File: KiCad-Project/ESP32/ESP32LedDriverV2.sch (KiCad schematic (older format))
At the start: 25 parts, among them J1 Power, J2 LED Terminal, Q1 Q_PMOS_GDS, Q2 S8050, U1 INA219AxD, U2 R-78C5.0-1.0

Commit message: swap out 603 resistors for 805
Give us more room to work with if we have to fix something.
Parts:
- R1: footprint Resistor_SMD:R_0603_1608Metric -> Resistor_SMD:R_0805_2012Metric; JLCPCB_PNUM C25804 -> C17414; MFG_PNUM 0603WAF1002T5E -> 0805W8F1002T5E; PACKAGE 0603 -> 0805
- R2, R4, R5, R6, R7: footprint Resistor_SMD:R_0201_0603Metric -> Resistor_SMD:R_0805_2012Metric; JLCPCB_PNUM C25804 -> C17414; MFG_PNUM 0603WAF1002T5E -> 0805W8F1002T5E; PACKAGE 0603 -> 0805
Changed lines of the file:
@@
 F 0 "R1" H 1643 1046 50  0000 L CNN
 F 1 "10K" H 1643 955 50  0000 L CNN
-F 2 "Resistor_SMD:R_0603_1608Metric" V 1615 990 50  0001 C CNN
+F 2 "Resistor_SMD:R_0805_2012Metric" V 1615 990 50  0001 C CNN
 F 3 "~" H 1575 1000 50  0001 C CNN
-F 4 "C25804" H 1575 1000 50  0001 C CNN "JLCPCB_PNUM"
-F 5 "0603WAF1002T5E" H 1575 1000 50  0001 C CNN "MFG_PNUM"
-F 6 "0603" H 1575 1000 50  0001 C CNN "PACKAGE"
+F 4 "C17414" H 1575 1000 50  0001 C CNN "JLCPCB_PNUM"
+F 5 "0805W8F1002T5E" H 1575 1000 50  0001 C CNN "MFG_PNUM"
+F 6 "0805" H 1575 1000 50  0001 C CNN "PACKAGE"
 F 7 "JLCPCB" H 1575 1000 50  0001 C CNN "SUPPLIER"
 	1    1575 1000
@@
 F 0 "R2" H 2443 1171 50  0000 L CNN
 F 1 "10K" H 2443 1080 50  0000 L CNN
-F 2 "Resistor_SMD:R_0201_0603Metric" V 2415 1115 50  0001 C CNN
+F 2 "Resistor_SMD:R_0805_2012Metric" V 2415 1115 50  0001 C CNN
 F 3 "~" H 2375 1125 50  0001 C CNN
-F 4 "C25804" H 2375 1125 50  0001 C CNN "JLCPCB_PNUM"
-F 5 "0603WAF1002T5E" H 2375 1125 50  0001 C CNN "MFG_PNUM"
-F 6 "0603" H 2375 1125 50  0001 C CNN "PACKAGE"
+F 4 "C17414" H 2375 1125 50  0001 C CNN "JLCPCB_PNUM"
+F 5 "0805W8F1002T5E" H 2375 1125 50  0001 C CNN "MFG_PNUM"
+F 6 "0805" H 2375 1125 50  0001 C CNN "PACKAGE"
 F 7 "JLCPCB" H 2375 1125 50  0001 C CNN "SUPPLIER"
 	1    2375 1125
@@
 F 0 "R5" H 3393 4396 50  0000 L CNN
 F 1 "10K" H 3393 4305 50  0000 L CNN
-F 2 "Resistor_SMD:R_0201_0603Metric" V 3365 4340 50  0001 C CNN
+F 2 "Resistor_SMD:R_0805_2012Metric" V 3365 4340 50  0001 C CNN
 F 3 "~" H 3325 4350 50  0001 C CNN
-F 4 "C25804" H 3325 4350 50  0001 C CNN "JLCPCB_PNUM"
-F 5 "0603WAF1002T5E" H 3325 4350 50  0001 C CNN "MFG_PNUM"
-F 6 "0603" H 3325 4350 50  0001 C CNN "PACKAGE"
+F 4 "C17414" H 3325 4350 50  0001 C CNN "JLCPCB_PNUM"
+F 5 "0805W8F1002T5E" H 3325 4350 50  0001 C CNN "MFG_PNUM"
+F 6 "0805" H 3325 4350 50  0001 C CNN "PACKAGE"
 F 7 "JLCPCB" H 3325 4350 50  0001 C CNN "SUPPLIER"
 	1    3325 4350
@@
 F 0 "R4" H 3018 4396 50  0000 L CNN
 F 1 "10K" H 3018 4305 50  0000 L CNN
-F 2 "Resistor_SMD:R_0201_0603Metric" V 2990 4340 50  0001 C CNN
+F 2 "Resistor_SMD:R_0805_2012Metric" V 2990 4340 50  0001 C CNN
 F 3 "~" H 2950 4350 50  0001 C CNN
-F 4 "C25804" H 2950 4350 50  0001 C CNN "JLCPCB_PNUM"
-F 5 "0603WAF1002T5E" H 2950 4350 50  0001 C CNN "MFG_PNUM"
-F 6 "0603" H 2950 4350 50  0001 C CNN "PACKAGE"
+F 4 "C17414" H 2950 4350 50  0001 C CNN "JLCPCB_PNUM"
+F 5 "0805W8F1002T5E" H 2950 4350 50  0001 C CNN "MFG_PNUM"
+F 6 "0805" H 2950 4350 50  0001 C CNN "PACKAGE"
 F 7 "JLCPCB" H 2950 4350 50  0001 C CNN "SUPPLIER"
 	1    2950 4350
@@
 F 0 "R6" V 3250 4875 50  0000 L CNN
 F 1 "10K" V 3418 4880 50  0000 L CNN
-F 2 "Resistor_SMD:R_0201_0603Metric" V 3390 4915 50  0001 C CNN
+F 2 "Resistor_SMD:R_0805_2012Metric" V 3390 4915 50  0001 C CNN
 F 3 "~" H 3350 4925 50  0001 C CNN
-F 4 "C25804" H 3350 4925 50  0001 C CNN "JLCPCB_PNUM"
-F 5 "0603WAF1002T5E" H 3350 4925 50  0001 C CNN "MFG_PNUM"
-F 6 "0603" H 3350 4925 50  0001 C CNN "PACKAGE"
+F 4 "C17414" H 3350 4925 50  0001 C CNN "JLCPCB_PNUM"
+F 5 "0805W8F1002T5E" H 3350 4925 50  0001 C CNN "MFG_PNUM"
+F 6 "0805" H 3350 4925 50  0001 C CNN "PACKAGE"
 F 7 "JLCPCB" H 3350 4925 50  0001 C CNN "SUPPLIER"
 	1    3350 4925
@@
 F 0 "R7" V 3250 5175 50  0000 L CNN
 F 1 "10K" V 3418 5180 50  0000 L CNN
-F 2 "Resistor_SMD:R_0201_0603Metric" V 3390 5215 50  0001 C CNN
+F 2 "Resistor_SMD:R_0805_2012Metric" V 3390 5215 50  0001 C CNN
 F 3 "~" H 3350 5225 50  0001 C CNN
-F 4 "C25804" H 3350 5225 50  0001 C CNN "JLCPCB_PNUM"
-F 5 "0603WAF1002T5E" H 3350 5225 50  0001 C CNN "MFG_PNUM"
-F 6 "0603" H 3350 5225 50  0001 C CNN "PACKAGE"
+F 4 "C17414" H 3350 5225 50  0001 C CNN "JLCPCB_PNUM"
+F 5 "0805W8F1002T5E" H 3350 5225 50  0001 C CNN "MFG_PNUM"
+F 6 "0805" H 3350 5225 50  0001 C CNN "PACKAGE"
 F 7 "JLCPCB" H 3350 5225 50  0001 C CNN "SUPPLIER"
 	1    3350 5225

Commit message: Switch power direction detection to SMD
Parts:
- removed Q2: S8050, Package_TO_SOT_SMD:SOT-23, symbol Transistor_BJT:BC337
- added Q2: S8050, Package_TO_SOT_SMD:SOT-23, symbol Transistor_BJT:BC817
- Q1: value Q_PMOS_GDS -> PMOS 30V; footprint Package_TO_SOT_THT:TO-220-3_Vertical -> Package_TO_SOT_SMD:SOT-23; JLCPCB_PNUM (none) -> C15127; MFG_PNUM (none) -> AO3401A; PACKAGE (none) -> SOT-23-3L; SUPPLIER Mouser -> JLCPCB
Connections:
- net GND: now also Q2.2 (E)
- net at Q1.1 (G), R1.2: now also Q2.3 (C)
- net at D1.1 (K), R2.2: now also Q2.1 (B)
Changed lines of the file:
@@
 P 2000 950
 F 0 "Q1" V 1900 825 50  0000 L CNN
-F 1 "Q_PMOS_GDS" V 2225 700 50  0000 L CNN
-F 2 "Package_TO_SOT_THT:TO-220-3_Vertical" H 2200 1050 50  0001 C CNN
-F 3 "~" H 2000 950 50  0001 C CNN
-F 4 "Mouser" H 2000 950 50  0001 C CNN "SUPPLIER"
+F 1 "PMOS 30V" V 2225 700 50  0000 L CNN
+F 2 "Package_TO_SOT_SMD:SOT-23" H 2200 1050 50  0001 C CNN
+F 3 "https://datasheet.lcsc.com/lcsc/1810171817_Alpha-&-Omega-Semicon-AO3401A_C15127.pdf" H 2000 950 50  0001 C CNN
+F 4 "JLCPCB" H 2000 950 50  0001 C CNN "SUPPLIER"
+F 5 "C15127" H 2000 950 50  0001 C CNN "JLCPCB_PNUM"
+F 6 "AO3401A" H 2000 950 50  0001 C CNN "MFG_PNUM"
+F 7 "SOT-23-3L" H 2000 950 50  0001 C CNN "PACKAGE"
 	1    2000 950
 	0    -1   -1   0
@@
 Wire Wire Line
 	1575 850  1450 850
-$Comp
-L Transistor_BJT:BC337 Q2
-U 1 1 61875D21
-P 2100 1425
-F 0 "Q2" H 2291 1471 50  0000 L CNN
-F 1 "S8050" H 2291 1380 50  0000 L CNN
-F 2 "Package_TO_SOT_SMD:SOT-23" H 2300 1350 50  0001 L CIN
-F 3 "https://diotec.com/tl_files/diotec/files/pdf/datasheets/bc337.pdf" H 2100 1425 50  0001 L CNN
-F 4 "C2146" H 2100 1425 50  0001 C CNN "JLCPCB_PNUM"
-F 5 "S8050 J3Y" H 2100 1425 50  0001 C CNN "MFG_PNUM"
-F 6 "SOT-23-3" H 2100 1425 50  0001 C CNN "PACKAGE"
-F 7 "JLCPCB" H 2100 1425 50  0001 C CNN "SUPPLIER"
-	1    2100 1425
-	-1   0    0    -1
-$EndComp
 Wire Wire Line
 	2000 1150 2000 1200
@@
 Wire Bus Line
 	6625 4450 6625 6500
+$Comp
+L Transistor_BJT:BC817 Q2
+U 1 1 61911107
+P 2100 1425
+F 0 "Q2" H 2291 1471 50  0000 L CNN
+F 1 "S8050" H 2291 1380 50  0000 L CNN
+F 2 "Package_TO_SOT_SMD:SOT-23" H 2300 1350 50  0001 L CIN
+F 3 "https://datasheet.lcsc.com/lcsc/1810161230_Changjiang-Electronics-Tech--CJ-S8050-J3Y_C2146.pdf" H 2100 1425 50  0001 L CNN
+F 4 "C2146" H 2100 1425 50  0001 C CNN "JLCPCB_PNUM"
+F 5 "S8050 J3Y" H 2100 1425 50  0001 C CNN "MFG_PNUM"
+F 6 "SOT-23-3" H 2100 1425 50  0001 C CNN "PACKAGE"
+F 7 "JLCPCB" H 2100 1425 50  0001 C CNN "SUPPLIER"
+	1    2100 1425
+	-1   0    0    -1
+$EndComp
 $EndSCHEMATC

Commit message: Fixes in prep for printing
Making sure tolerance are in-spec for JLC PCB
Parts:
- D1: MFG_PNUM M7 -> MDD - M7
- D2: footprint Diode_THT:D_DO-34_SOD68_P7.62mm_Horizontal -> Diode_THT:D_DO-35_SOD27_P7.62mm_Horizontal; MFG_PNUM (none) -> 1N5253B-TAP; PACKAGE (none) -> DO-35-2
- R3: value 100 ±1% 1W -> 0.1Ω 1% 1W
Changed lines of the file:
@@
 F 1 "D" V 2420 1655 50  0000 L CNN
 F 2 "Diode_SMD:D_SMA" H 2375 1575 50  0001 C CNN
-F 3 "~" H 2375 1575 50  0001 C CNN
+F 3 "https://datasheet.lcsc.com/lcsc/1810311713_MDD%EF%BC%88Microdiode-Electronics%EF%BC%89-M7_C95872.pdf" H 2375 1575 50  0001 C CNN
 F 4 "C95872" H 2375 1575 50  0001 C CNN "JLCPCB_PNUM"
-F 5 "M7" H 2375 1575 50  0001 C CNN "MFG_PNUM"
+F 5 "MDD - M7" H 2375 1575 50  0001 C CNN "MFG_PNUM"
 F 6 "SMA,DO-214AC" H 2375 1575 50  0001 C CNN "PACKAGE"
 F 7 "JLCPCB" H 2375 1575 50  0001 C CNN "SUPPLIER"
@@
 F 1 "0.1uF" H 1790 4130 50  0000 L CNN
 F 2 "Capacitor_SMD:C_0805_2012Metric" H 1713 4025 50  0001 C CNN
-F 3 "~" H 1675 4175 50  0001 C CNN
+F 3 "https://datasheet.lcsc.com/lcsc/1810101813_YAGEO-CC0805KRX7R9BB104_C49678.pdf" H 1675 4175 50  0001 C CNN
 F 4 "C49678" H 1675 4175 50  0001 C CNN "JLCPCB_PNUM"
 F 5 "CC0805KRX7R9BB104" H 1675 4175 50  0001 C CNN "MFG_PNUM"
@@
 P 1325 5350
 F 0 "R3" V 1225 5300 50  0000 L CNN
-F 1 "100 ±1% 1W " H 1375 5375 50  0000 L CNN
+F 1 "0.1Ω 1% 1W" H 1375 5375 50  0000 L CNN
 F 2 "Resistor_SMD:R_2512_6332Metric" V 1365 5340 50  0001 C CNN
-F 3 "~" H 1325 5350 50  0001 C CNN
+F 3 "https://datasheet.lcsc.com/lcsc/1811081330_RALEC-LR2512-21R100F4_C154665.pdf" H 1325 5350 50  0001 C CNN
 F 4 "C154665" H 1325 5350 50  0001 C CNN "JLCPCB_PNUM"
 F 5 "LR2512-21R100F4" H 1325 5350 50  0001 C CNN "MFG_PNUM"
@@
 F 0 "D2" V 1404 3005 50  0000 L CNN
 F 1 "D_Zener 25v" V 1495 3005 50  0000 L CNN
-F 2 "Diode_THT:D_DO-34_SOD68_P7.62mm_Horizontal" H 1450 2925 50  0001 C CNN
+F 2 "Diode_THT:D_DO-35_SOD27_P7.62mm_Horizontal" H 1450 2925 50  0001 C CNN
 F 3 "~" H 1450 2925 50  0001 C CNN
 F 4 "Mouser" H 1450 2925 50  0001 C CNN "SUPPLIER"
+F 5 "1N5253B-TAP" H 1450 2925 50  0001 C CNN "MFG_PNUM"
+F 6 "DO-35-2" H 1450 2925 50  0001 C CNN "PACKAGE"
 	1    1450 2925
 	0    1    1    0
@@
 Wire Wire Line
 	2525 6900 2975 6900
-Wire Bus Line
-	9025 1875 9025 4150
-Wire Bus Line
-	8300 1875 8300 6275
-Wire Bus Line
-	7125 2050 7125 6500
-Wire Bus Line
-	6625 4450 6625 6500
 $Comp
 L Transistor_BJT:BC817 Q2
@@
 	-1   0    0    -1
 $EndComp
+Wire Bus Line
+	9025 1875 9025 4150
+Wire Bus Line
+	8300 1875 8300 6275
+Wire Bus Line
+	7125 2050 7125 6500
+Wire Bus Line
+	6625 4450 6625 6500
 $EndSCHEMATC

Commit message: Fix Power Mosfet direction
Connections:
- net +24V_RAW: now also Q1.3 (S); no longer Q1.2 (D)
- net +24V_SW: now also Q1.2 (D); no longer Q1.3 (S)
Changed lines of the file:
@@
 F 7 "SOT-23-3L" H 2000 950 50  0001 C CNN "PACKAGE"
 	1    2000 950
-	0    -1   -1   0
+	0    1    -1   0
 $EndComp
 Wire Wire Line

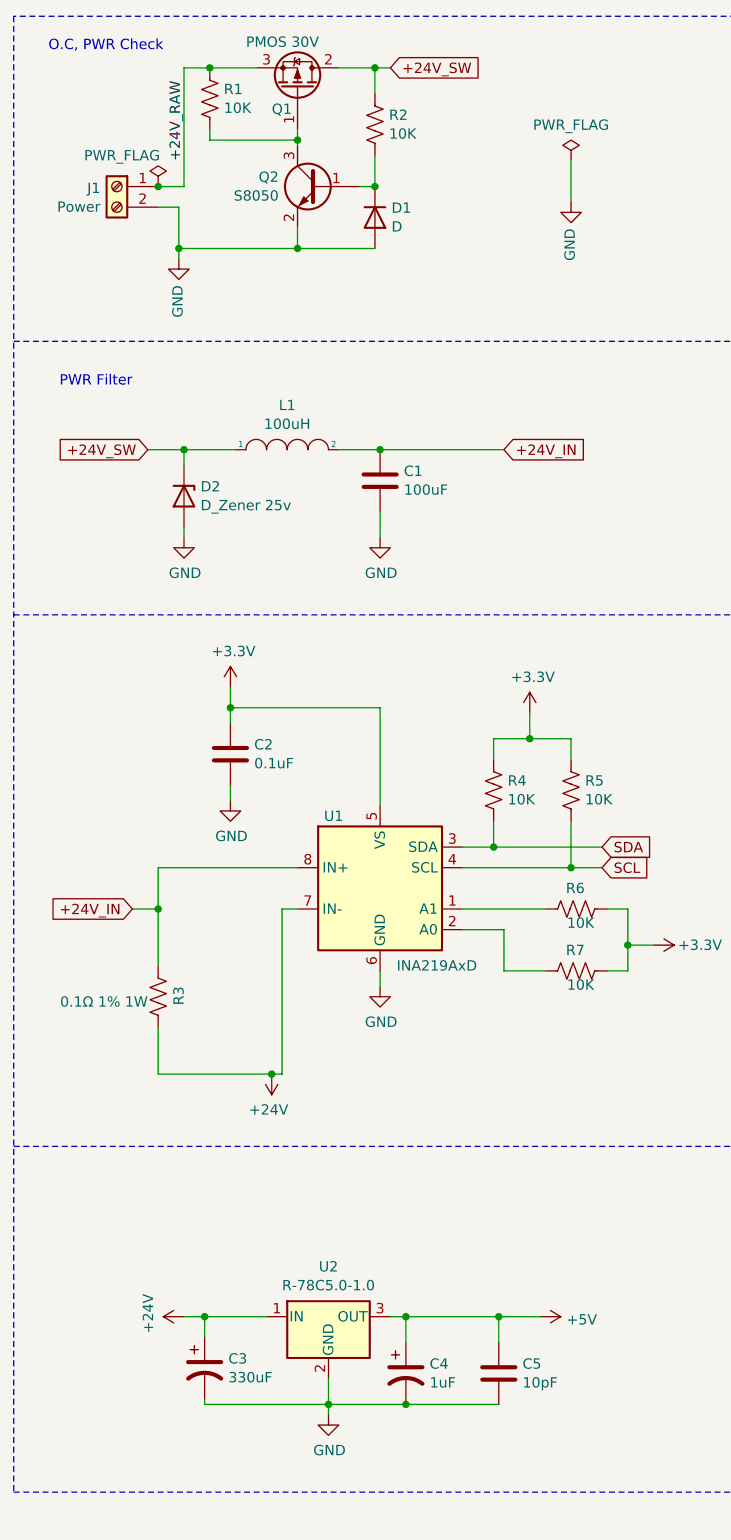
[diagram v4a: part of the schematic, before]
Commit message: Removed reverse voltage and increased size of power traces
Reverse voltage needed different components for 24 volt, and was a nice to have, so to keep cost down, opted to remove it.
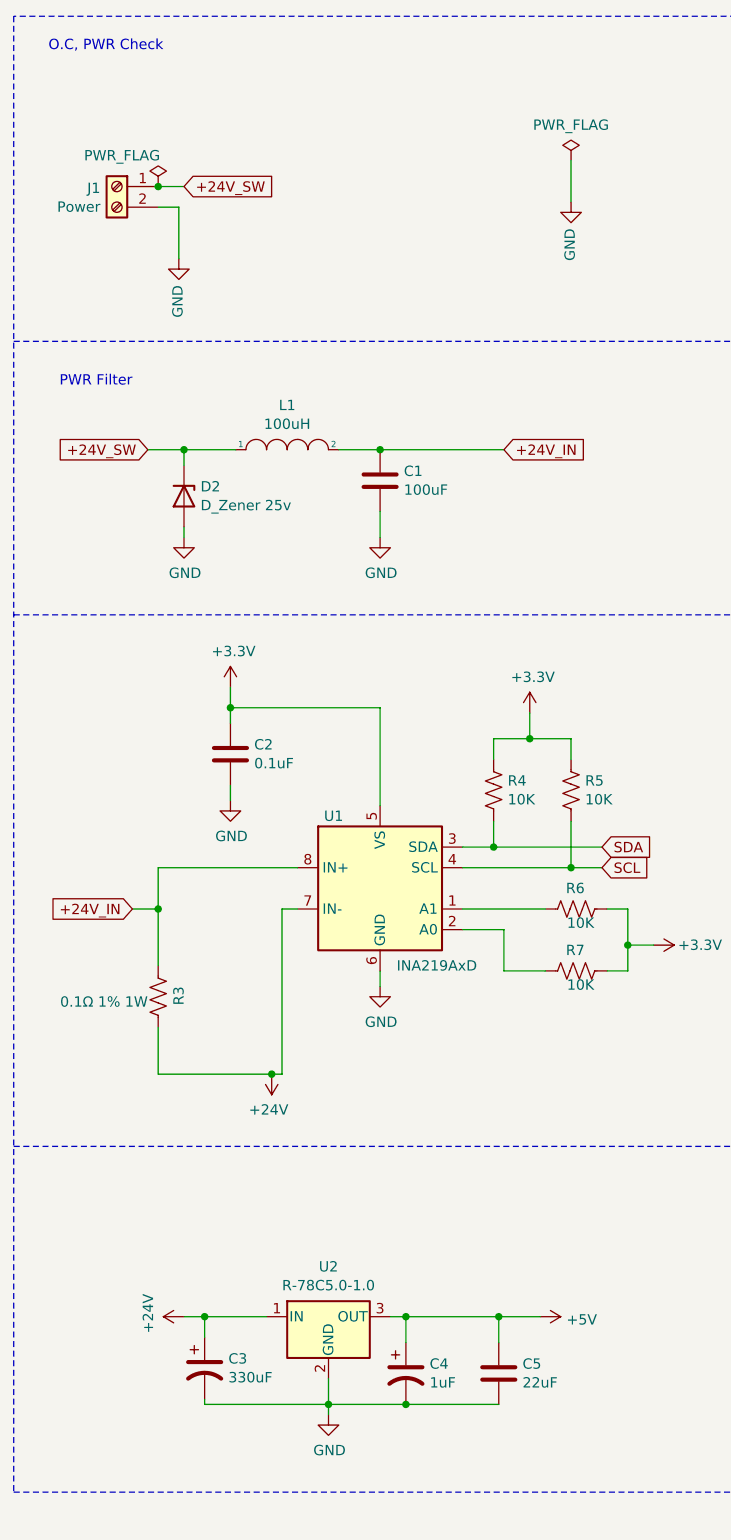
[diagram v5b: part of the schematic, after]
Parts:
- removed D1: D, Diode_SMD:D_SMA, symbol Device:D
- removed Q1: PMOS 30V, Package_TO_SOT_SMD:SOT-23, symbol Device:Q_PMOS_GDS
- removed Q2: S8050, Package_TO_SOT_SMD:SOT-23, symbol Transistor_BJT:BC817
- removed R1, R2: 10K, Resistor_SMD:R_0805_2012Metric, symbol Device:R_US
- C5: value 10pF -> 22uF; JLCPCB_PNUM C1785 -> C45783; MFG_PNUM CL21C100JBANNNC -> CL21A226MAQNNNE
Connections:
- net +24V_RAW is gone; now on net +24V_SW: J1.1 (Pin_1)
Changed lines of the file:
@@
 Entry Wire Line
 	7125 2800 7225 2700
-$Comp
-L Device:Q_PMOS_GDS Q1
-U 1 1 61841478
-P 2000 950
-F 0 "Q1" V 1900 825 50  0000 L CNN
-F 1 "PMOS 30V" V 2225 700 50  0000 L CNN
-F 2 "Package_TO_SOT_SMD:SOT-23" H 2200 1050 50  0001 C CNN
-F 3 "https://datasheet.lcsc.com/lcsc/1810171817_Alpha-&-Omega-Semicon-AO3401A_C15127.pdf" H 2000 950 50  0001 C CNN
-F 4 "JLCPCB" H 2000 950 50  0001 C CNN "SUPPLIER"
-F 5 "C15127" H 2000 950 50  0001 C CNN "JLCPCB_PNUM"
-F 6 "AO3401A" H 2000 950 50  0001 C CNN "MFG_PNUM"
-F 7 "SOT-23-3L" H 2000 950 50  0001 C CNN "PACKAGE"
-	1    2000 950
-	0    1    -1   0
-$EndComp
-Wire Wire Line
-	2200 850  2375 850
-Wire Wire Line
-	1800 850  1575 850
-Wire Wire Line
-	1450 850  1450 1425
 Wire Wire Line
 	1450 1425 1325 1425
-$Comp
-L Device:R_US R1
-U 1 1 61872076
-P 1575 1000
-F 0 "R1" H 1643 1046 50  0000 L CNN
-F 1 "10K" H 1643 955 50  0000 L CNN
-F 2 "Resistor_SMD:R_0805_2012Metric" V 1615 990 50  0001 C CNN
-F 3 "~" H 1575 1000 50  0001 C CNN
-F 4 "C17414" H 1575 1000 50  0001 C CNN "JLCPCB_PNUM"
-F 5 "0805W8F1002T5E" H 1575 1000 50  0001 C CNN "MFG_PNUM"
-F 6 "0805" H 1575 1000 50  0001 C CNN "PACKAGE"
-F 7 "JLCPCB" H 1575 1000 50  0001 C CNN "SUPPLIER"
-	1    1575 1000
-	1    0    0    -1
-$EndComp
-Connection ~ 1575 850
-Wire Wire Line
-	1575 850  1450 850
-Wire Wire Line
-	2000 1150 2000 1200
 Wire Wire Line
 	1325 1525 1425 1525
-Wire Wire Line
-	1575 1150 1575 1200
-Wire Wire Line
-	1575 1200 2000 1200
-Connection ~ 2000 1200
-Wire Wire Line
-	2000 1200 2000 1225
-Wire Wire Line
-	2000 1725 1425 1725
-$Comp
-L Device:D D1
-U 1 1 6188E2F7
-P 2375 1575
-F 0 "D1" V 2329 1655 50  0000 L CNN
-F 1 "D" V 2420 1655 50  0000 L CNN
-F 2 "Diode_SMD:D_SMA" H 2375 1575 50  0001 C CNN
-F 3 "https://datasheet.lcsc.com/lcsc/1810311713_MDD%EF%BC%88Microdiode-Electronics%EF%BC%89-M7_C95872.pdf" H 2375 1575 50  0001 C CNN
-F 4 "C95872" H 2375 1575 50  0001 C CNN "JLCPCB_PNUM"
-F 5 "MDD - M7" H 2375 1575 50  0001 C CNN "MFG_PNUM"
-F 6 "SMA,DO-214AC" H 2375 1575 50  0001 C CNN "PACKAGE"
-F 7 "JLCPCB" H 2375 1575 50  0001 C CNN "SUPPLIER"
-	1    2375 1575
-	0    1    1    0
-$EndComp
-Wire Wire Line
-	2375 1425 2300 1425
-Wire Wire Line
-	2375 1725 2000 1725
-Connection ~ 1425 1725
-Wire Wire Line
-	1425 1725 1425 1775
-Connection ~ 2000 1725
-Wire Wire Line
-	1425 1525 1425 1725
-Wire Wire Line
-	2000 1625 2000 1725
-$Comp
-L Device:R_US R2
-U 1 1 61896021
-P 2375 1125
-F 0 "R2" H 2443 1171 50  0000 L CNN
-F 1 "10K" H 2443 1080 50  0000 L CNN
-F 2 "Resistor_SMD:R_0805_2012Metric" V 2415 1115 50  0001 C CNN
-F 3 "~" H 2375 1125 50  0001 C CNN
-F 4 "C17414" H 2375 1125 50  0001 C CNN "JLCPCB_PNUM"
-F 5 "0805W8F1002T5E" H 2375 1125 50  0001 C CNN "MFG_PNUM"
-F 6 "0805" H 2375 1125 50  0001 C CNN "PACKAGE"
-F 7 "JLCPCB" H 2375 1125 50  0001 C CNN "SUPPLIER"
-	1    2375 1125
-	1    0    0    -1
-$EndComp
-Wire Wire Line
-	2375 975  2375 850
-Connection ~ 2375 1425
-Wire Wire Line
-	2375 1275 2375 1425
 Text GLabel 3475 4625 2    50   Input ~ 0
 SDA
@@
 P 2975 7175
 F 0 "C5" H 3090 7221 50  0000 L CNN
-F 1 "10pF" H 3090 7130 50  0000 L CNN
+F 1 "22uF" H 3090 7130 50  0000 L CNN
 F 2 "Capacitor_SMD:C_0805_2012Metric" H 3013 7025 50  0001 C CNN
 F 3 "~" H 2975 7175 50  0001 C CNN
-F 4 "C1785" H 2975 7175 50  0001 C CNN "JLCPCB_PNUM"
-F 5 "CL21C100JBANNNC" H 2975 7175 50  0001 C CNN "MFG_PNUM"
+F 4 "C45783" H 2975 7175 50  0001 C CNN "JLCPCB_PNUM"
+F 5 "CL21A226MAQNNNE" H 2975 7175 50  0001 C CNN "MFG_PNUM"
 F 6 "0805" H 2975 7175 50  0001 C CNN "PACKAGE"
 F 7 "JLCPCB" H 2975 7175 50  0001 C CNN "SUPPLIER"
@@
 Wire Wire Line
 	1325 5200 1325 4925
-Text Label 1450 1300 1    50   ~ 0
-+24V_RAW
 $Comp
 L Mechanical:MountingHole H2
@@
 	1    0    0    -1
 $EndComp
-Text GLabel 2450 850  2    50   Input ~ 0
+Text GLabel 1450 1425 2    50   Input ~ 0
 +24V_SW
 Text Notes 1350 775  2    50   ~ 0
 O.C, PWR Check
-Wire Wire Line
-	2375 850  2450 850
-Connection ~ 2375 850
 Text Notes 1200 2400 2    50   ~ 0
 PWR Filter
@@
 Wire Wire Line
 	2525 6900 2975 6900
-$Comp
-L Transistor_BJT:BC817 Q2
-U 1 1 61911107
-P 2100 1425
-F 0 "Q2" H 2291 1471 50  0000 L CNN
-F 1 "S8050" H 2291 1380 50  0000 L CNN
-F 2 "Package_TO_SOT_SMD:SOT-23" H 2300 1350 50  0001 L CIN
-F 3 "https://datasheet.lcsc.com/lcsc/1810161230_Changjiang-Electronics-Tech--CJ-S8050-J3Y_C2146.pdf" H 2100 1425 50  0001 L CNN
-F 4 "C2146" H 2100 1425 50  0001 C CNN "JLCPCB_PNUM"
-F 5 "S8050 J3Y" H 2100 1425 50  0001 C CNN "MFG_PNUM"
-F 6 "SOT-23-3" H 2100 1425 50  0001 C CNN "PACKAGE"
-F 7 "JLCPCB" H 2100 1425 50  0001 C CNN "SUPPLIER"
-	1    2100 1425
-	-1   0    0    -1
-$EndComp
+Wire Wire Line
+	1425 1525 1425 1775
 Wire Bus Line
 	9025 1875 9025 4150
